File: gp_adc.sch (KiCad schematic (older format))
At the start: 26 parts, among them U33 INA199C2DCKT, U6 ADS7952SRHBT, U7 OPA202, U8 REF5025AIDR

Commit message: cleanup from Eagle import
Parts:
- removed H1, H2, H3, H4: MOUNT-HOLE3.0, adc_dac_v1:3,0, symbol adc_dac_v1-eagle-import:MOUNT-HOLE3.0
- C1, C2, C21, C22, C25, C26, C45, C51: footprint adc_dac_v1:C0603 -> Capacitor_SMD:C_0603_1608Metric; symbol adc_dac_v1-eagle-import:C-USC0603 -> Device:C
- R132, R134, R135, R136, R137, R23, R24, R65: footprint adc_dac_v1:R0603 -> Resistor_SMD:R_0603_1608Metric; symbol adc_dac_v1-eagle-import:R-US_R0603 -> Device:R_US
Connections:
- net labels added: +3V3, +5V
- net labels removed: 3V3, 5V
- wire segments 99 -> 107
- no-connect marks 0 -> 4

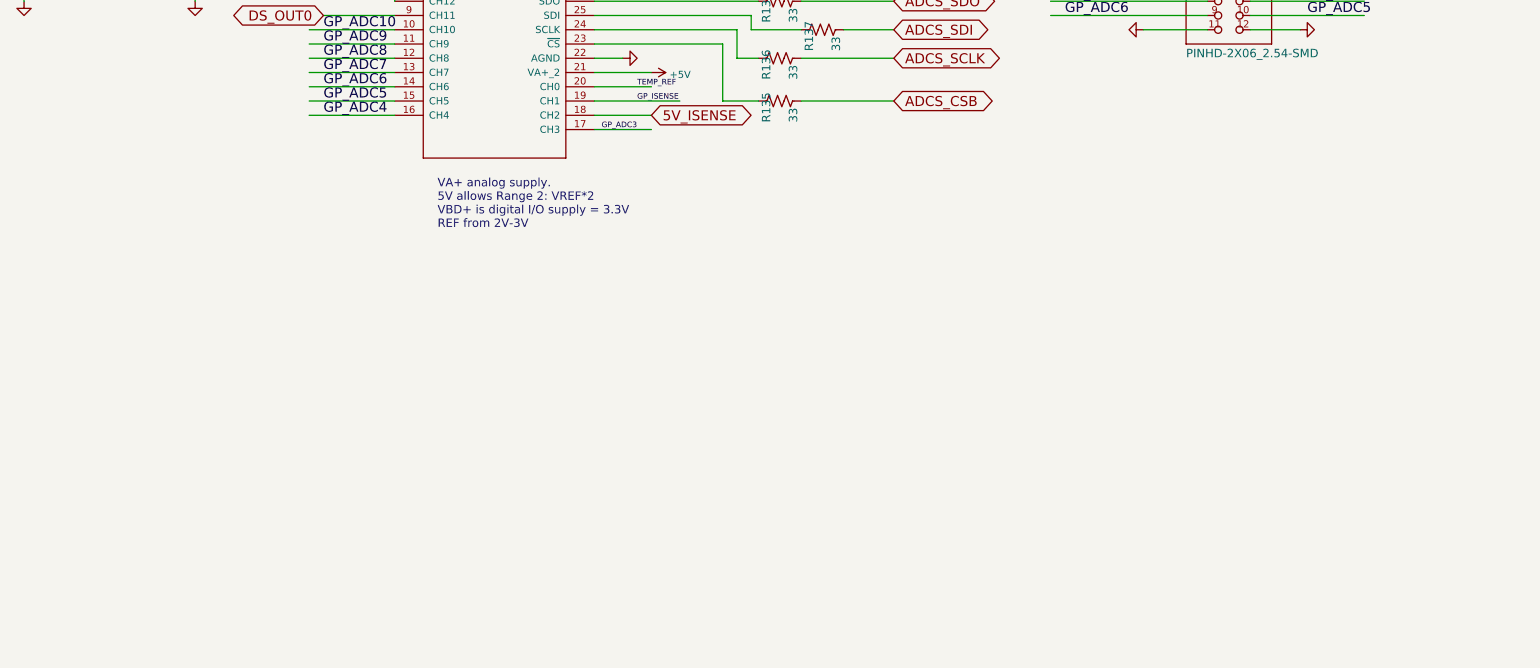
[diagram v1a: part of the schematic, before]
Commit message: added different general purpose ADC
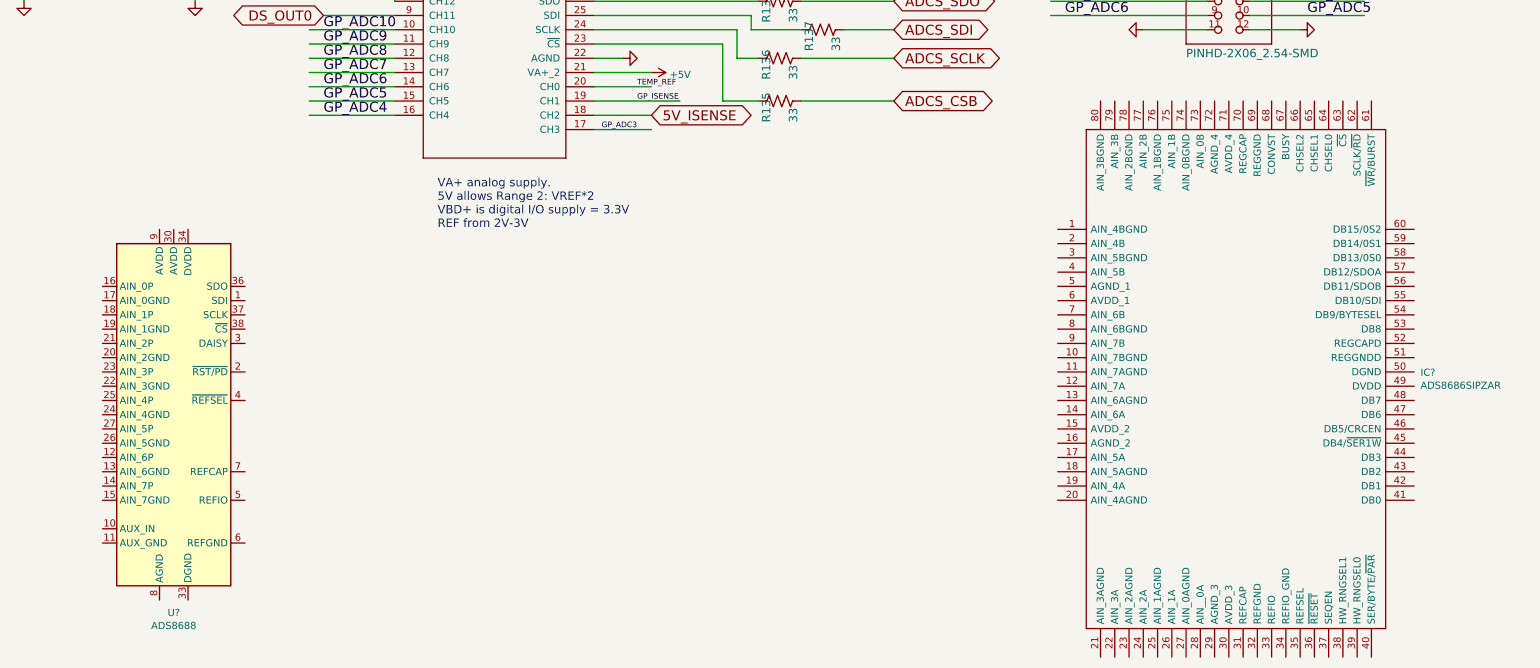
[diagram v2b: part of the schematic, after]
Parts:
- added IC?: ADS8686SIPZAR, QFP65P1600X1600X160-80N, symbol covg-kicad:ADS8686SIPZAR
- added U?: ADS8688, Package_SO:TSSOP-38_4.4x9.7mm_P0.5mm, symbol Analog_ADC:ADS8688
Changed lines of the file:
@@
 Wire Wire Line
 	3000 3950 3000 4000
+$Comp
+L Analog_ADC:ADS8688 U?
+U 1 1 609DAA3D
+P 2850 7800
+F 0 "U?" H 2850 6411 50  0000 C CNN
+F 1 "ADS8688" H 2850 6320 50  0000 C CNN
+F 2 "Package_SO:TSSOP-38_4.4x9.7mm_P0.5mm" H 2850 7800 50  0001 C CNN
+F 3 "http://www.ti.com/lit/ds/symlink/ads8688.pdf" H 3800 9100 50  0001 C CNN
+	1    2850 7800
+	1    0    0    -1
+$EndComp
+$Comp
+L covg-kicad:ADS8686SIPZAR IC?
+U 1 1 609E17A7
+P 9050 6500
+F 0 "IC?" H 11594 5496 50  0000 L CNN
+F 1 "ADS8686SIPZAR" H 11594 5405 50  0000 L CNN
+F 2 "QFP65P1600X1600X160-80N" H 11400 7200 50  0001 L CNN
+F 3 "https://www.ti.com/lit/gpn/ADS8686S" H 11400 7100 50  0001 L CNN
+F 4 "Analog to Digital Converters - ADC 16-channel 16-bit 1-MSPS dual simultaneous-sampling ADC with integrated analog front end (AFE)" H 11400 7000 50  0001 L CNN "Description"
+F 5 "1.6" H 11400 6900 50  0001 L CNN "Height"
+F 6 "Texas Instruments" H 11400 6800 50  0001 L CNN "Manufacturer_Name"
+F 7 "ADS8686SIPZAR" H 11400 6700 50  0001 L CNN "Manufacturer_Part_Number"
+F 8 "595-ADS8686SIPZAR" H 11400 6600 50  0001 L CNN "Mouser Part Number"
+F 9 "https://www.mouser.co.uk/ProductDetail/Texas-Instruments/ADS8686SIPZAR/?qs=xZ%2FP%252Ba9zWqahOWZgBjtpsg%3D%3D" H 11400 6500 50  0001 L CNN "Mouser Price/Stock"
+F 10 "" H 11400 6400 50  0001 L CNN "Arrow Part Number"
+F 11 "" H 11400 6300 50  0001 L CNN "Arrow Price/Stock"
+	1    9050 6500
+	1    0    0    -1
+$EndComp
 $EndSCHEMATC

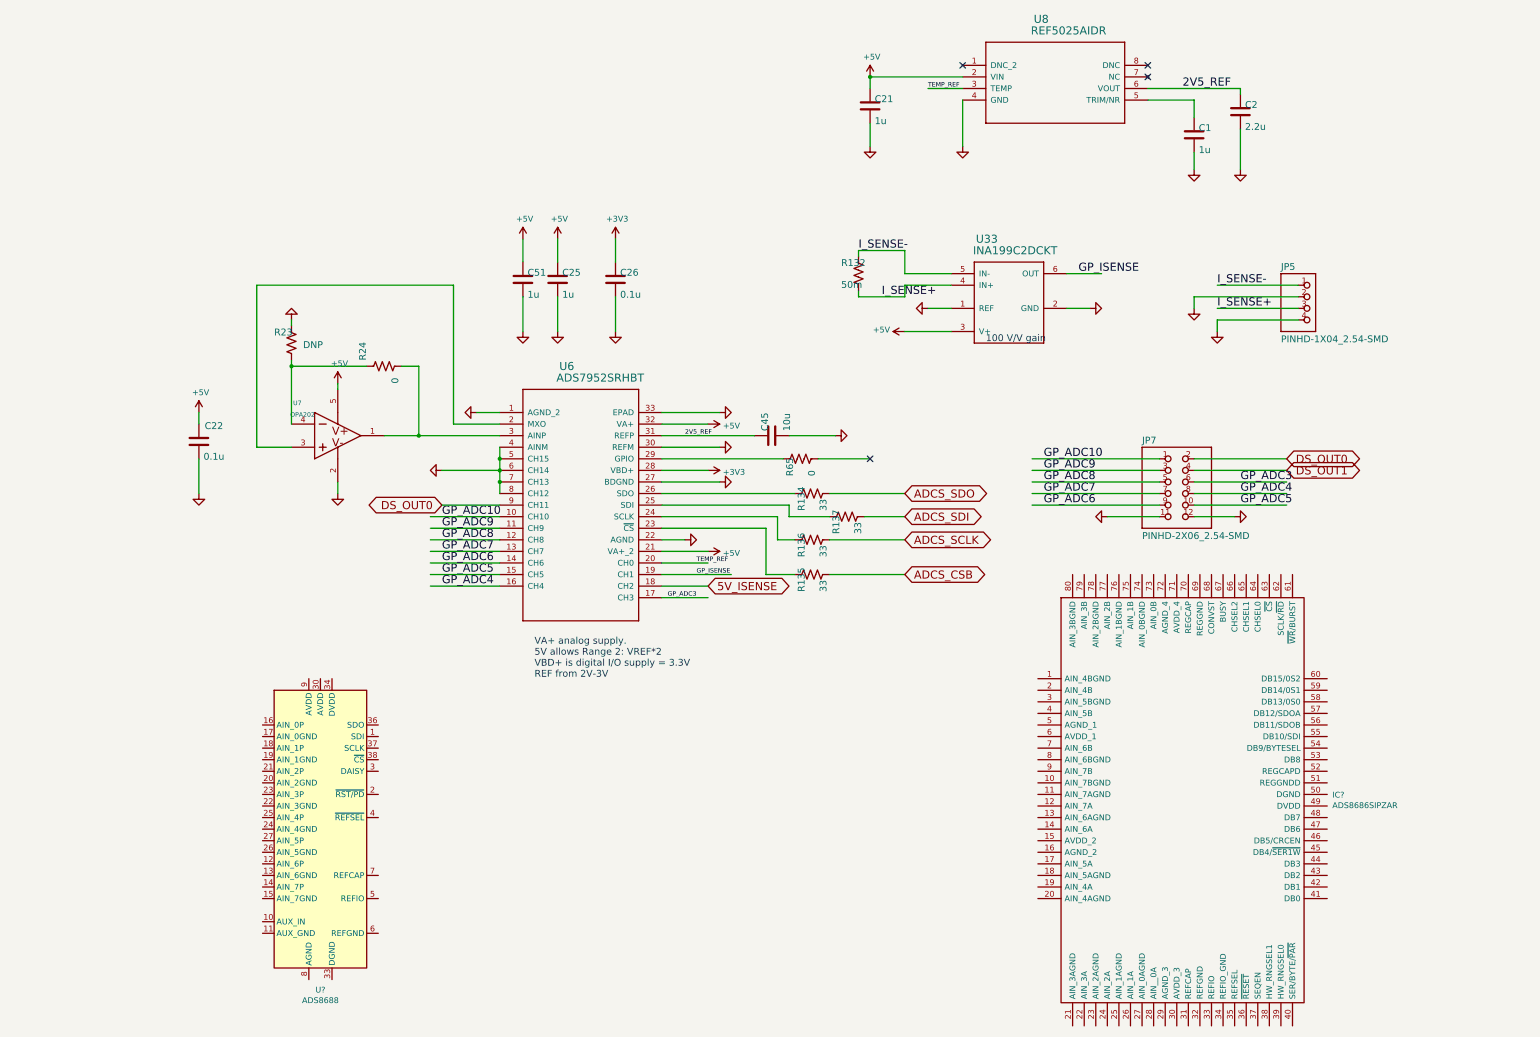
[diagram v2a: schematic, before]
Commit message: edits to general purpose DAC and gp ADC
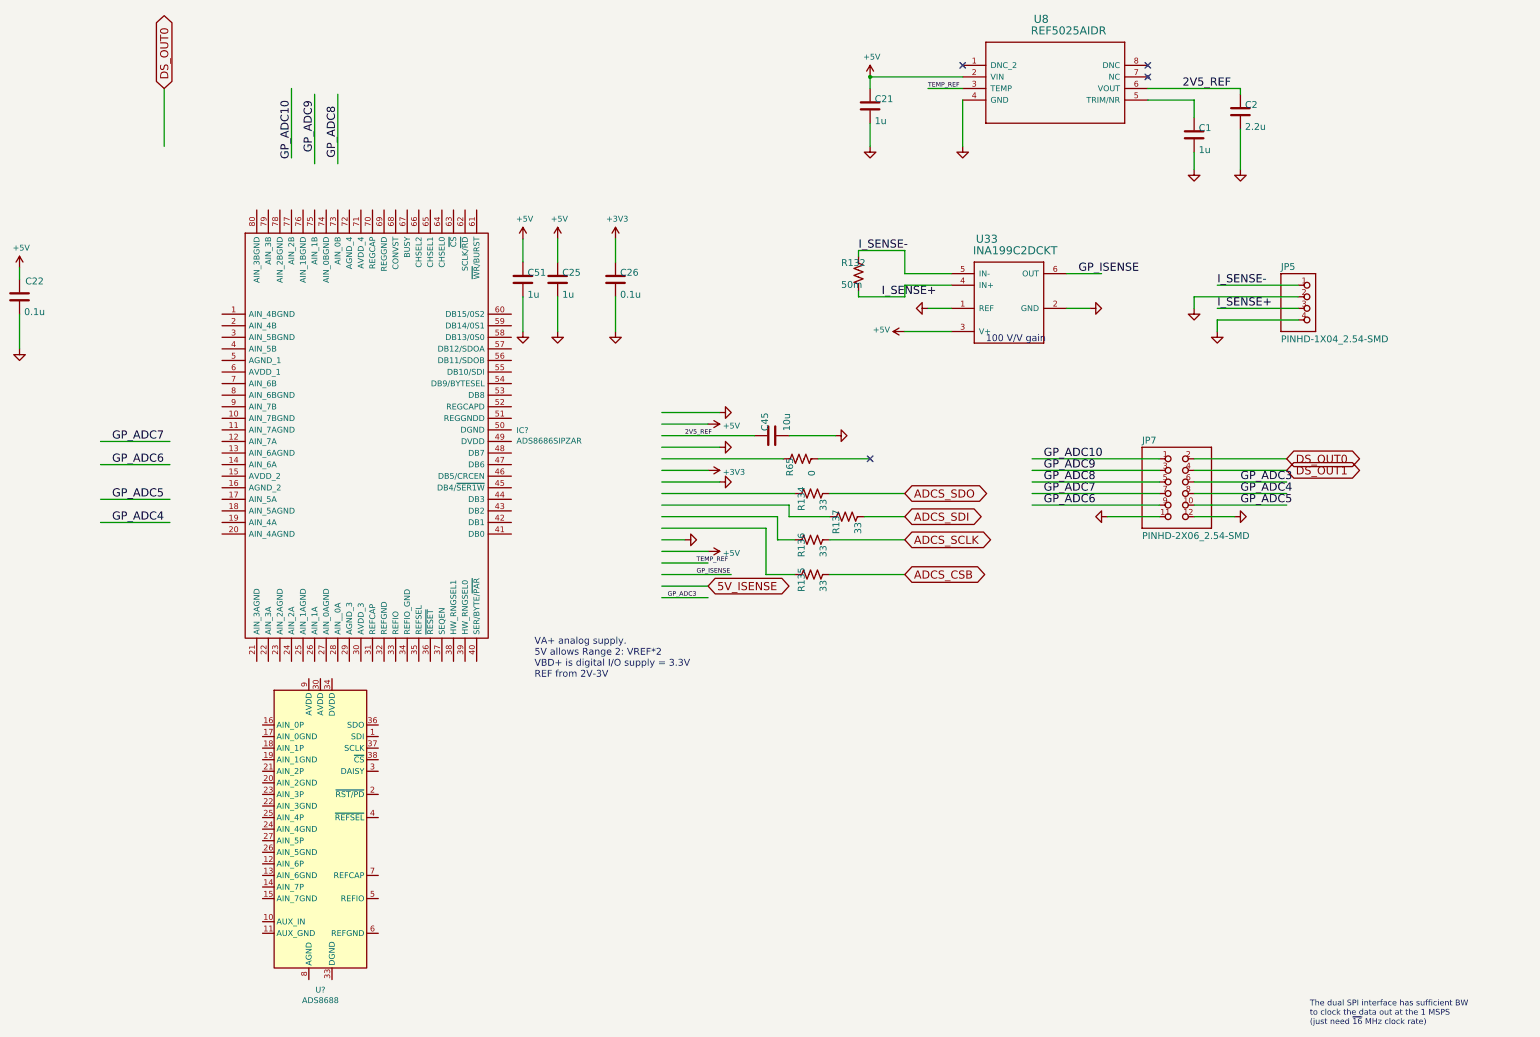
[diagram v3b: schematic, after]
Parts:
- removed R23: DNP, Resistor_SMD:R_0603_1608Metric, symbol Device:R_US
- removed R24: 0, Resistor_SMD:R_0603_1608Metric, symbol Device:R_US
- removed U6: ADS7952SRHBT, adc_dac_v1:RHB32_2P7X2P7_TEX, symbol adc_dac_v1-eagle-import:ADS7952SRHBT
- removed U7: OPA202, adc_dac_v1:DBV0005A_N, symbol adc_dac_v1-eagle-import:OPA192IDBVR
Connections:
- wire segments 107 -> 86
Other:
- note added: "The dual SPI interface has sufficient BW \nto clock the data out at the 1 MSPS \n(just need ~16 MHz clock rate)"
- moved on the sheet: C22, IC?

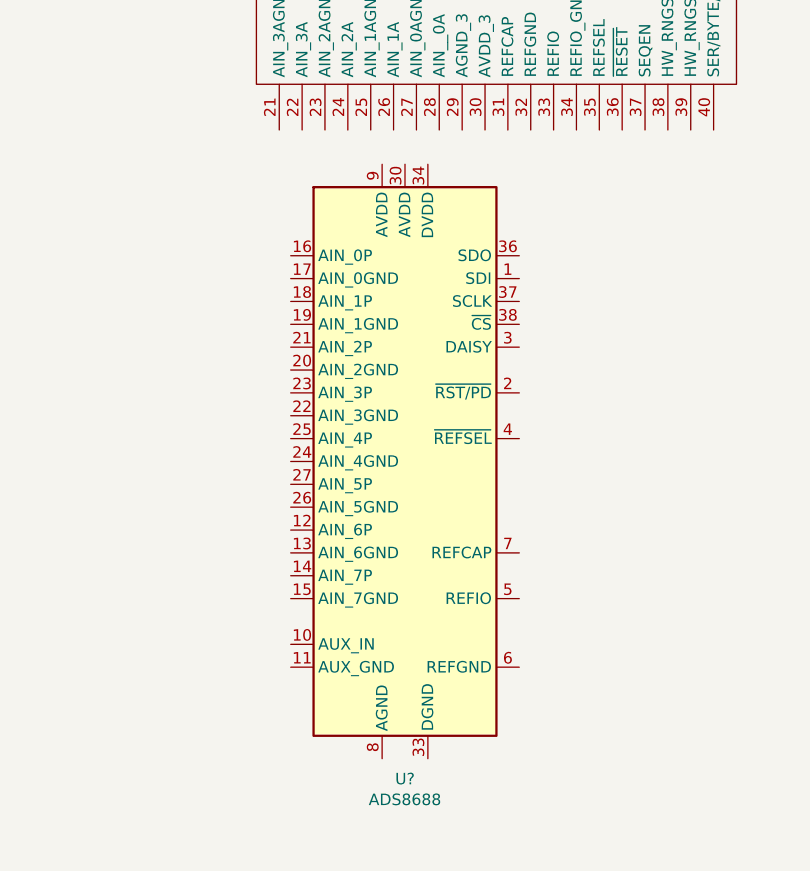
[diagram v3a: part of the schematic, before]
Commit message: updates to README
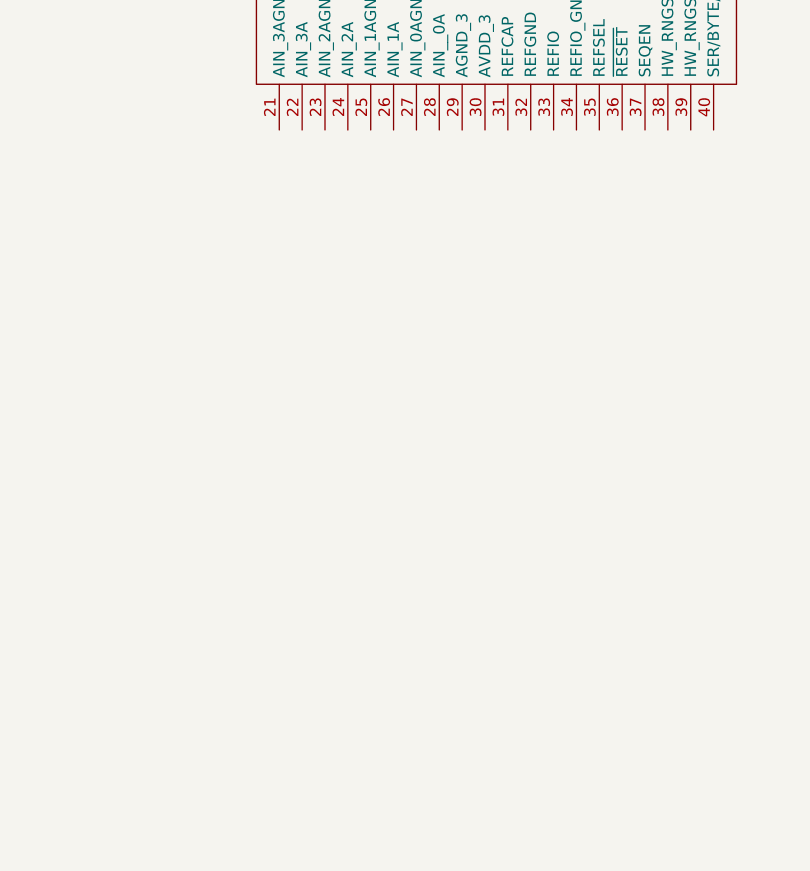
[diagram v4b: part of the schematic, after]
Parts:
- removed U?: ADS8688, Package_SO:TSSOP-38_4.4x9.7mm_P0.5mm, symbol Analog_ADC:ADS8688
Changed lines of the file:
@@
 NoConn ~ 8400 1200
-$Comp
-L Analog_ADC:ADS8688 U?
-U 1 1 609DAA3D
-P 2850 7800
-F 0 "U?" H 2850 6411 50  0000 C CNN
-F 1 "ADS8688" H 2850 6320 50  0000 C CNN
-F 2 "Package_SO:TSSOP-38_4.4x9.7mm_P0.5mm" H 2850 7800 50  0001 C CNN
-F 3 "http://www.ti.com/lit/ds/symlink/ads8688.pdf" H 3800 9100 50  0001 C CNN
-	1    2850 7800
-	1    0    0    -1
-$EndComp
 $Comp
 L covg-kicad:ADS8686SIPZAR IC?
